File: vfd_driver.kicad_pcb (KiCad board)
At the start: 2 copper layers, 41.1 x 26.7 mm, 23 parts, among them J1 INPUT, J2 FIL, J3 HV, U1 LM4871, U2 LT1073CS

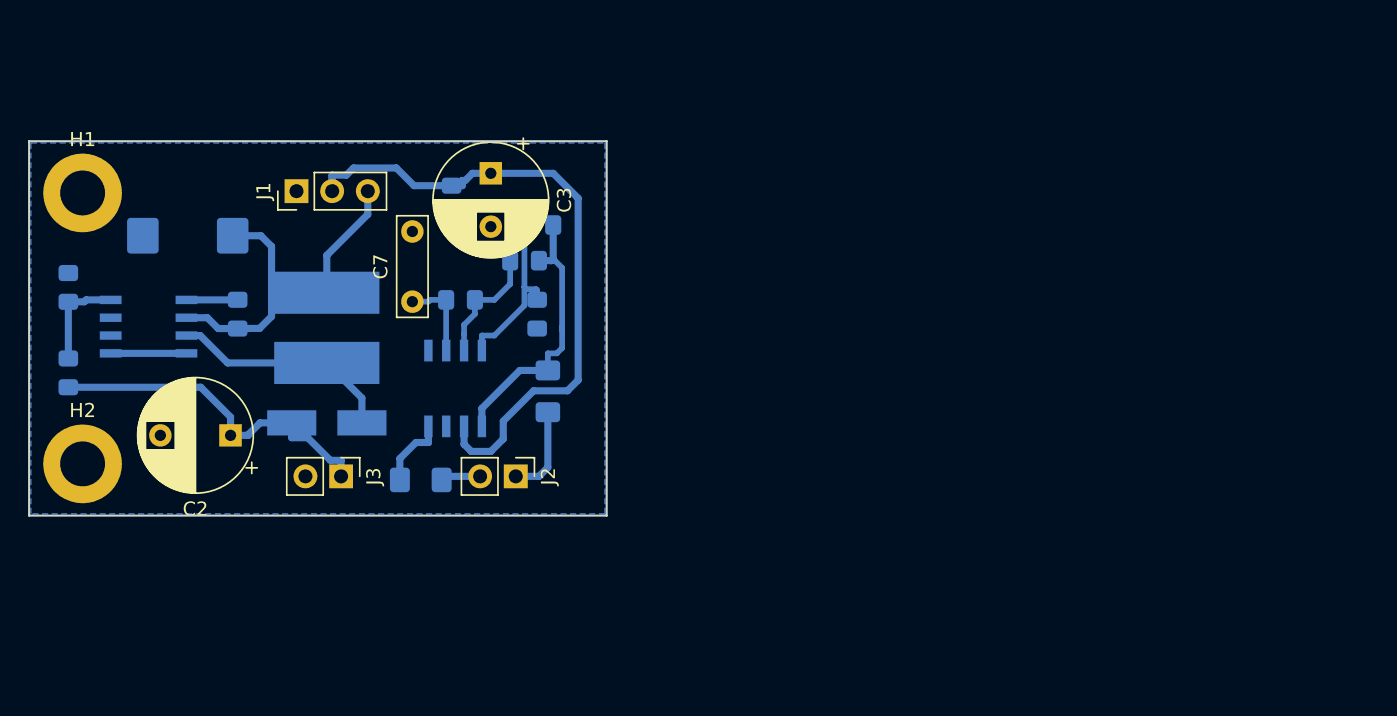
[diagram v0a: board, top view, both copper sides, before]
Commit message: add a protecting diode to the power input. make sure the right thing are pushed.
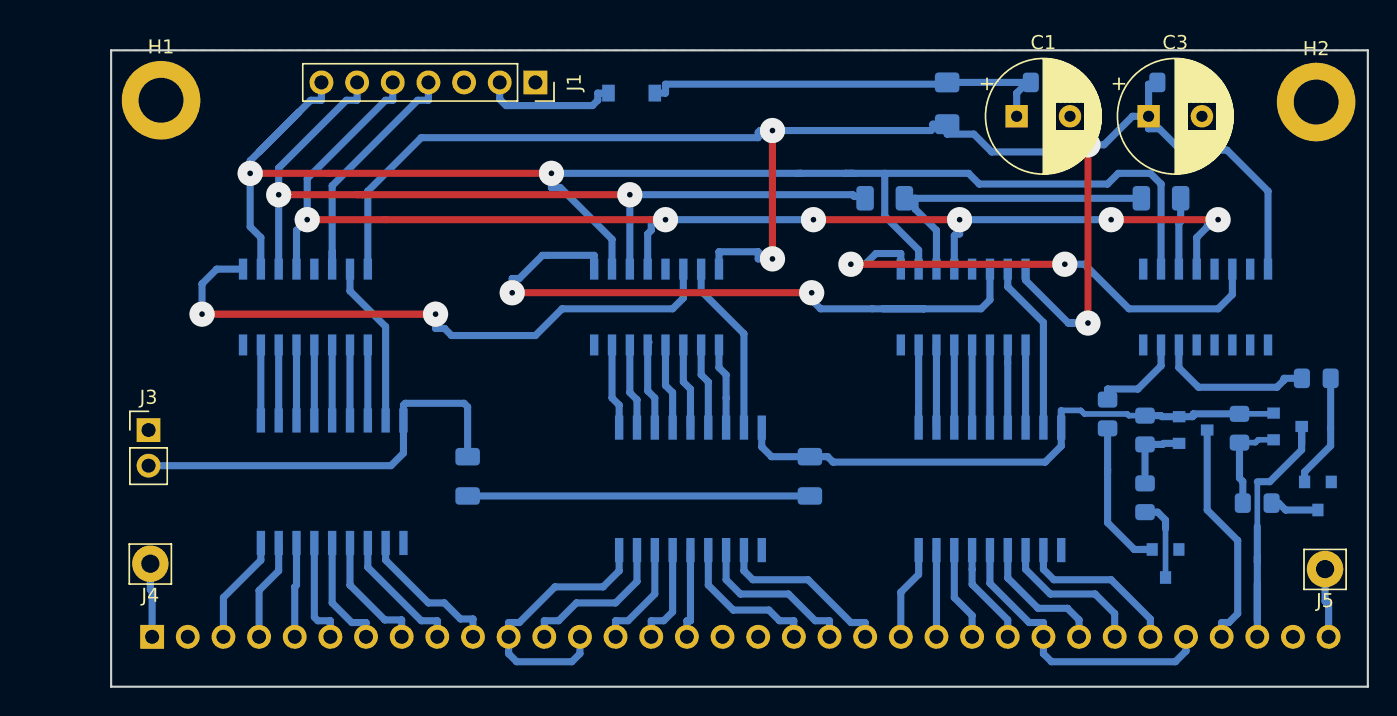
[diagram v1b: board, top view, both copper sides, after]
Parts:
- removed C6: 4n7, Capacitor_SMD:C_0805_2012Metric_Pad1.15x1.40mm_HandSolder
- removed C7: 1u, Capacitor_THT:C_Rect_L7.0mm_W2.0mm_P5.00mm
- removed L1: 330, Choke_SMD:Choke_CD75
- removed R15, R3: 22k, Resistor_SMD:R_0805_2012Metric_Pad1.15x1.40mm_HandSolder
- removed R16, R17: 18, Resistor_SMD:R_1206_3216Metric_Pad1.42x1.75mm_HandSolder
- removed R4: 10k, Resistor_SMD:R_0805_2012Metric_Pad1.15x1.40mm_HandSolder
- added J4: FIL_n, Connector_Pin:Pin_D1.4mm_L8.5mm_W2.8mm_FlatFork, F.Cu at (36.4, 65.5)
- added J5: FIL_p, Connector_Pin:Pin_D1.4mm_L8.5mm_W2.8mm_FlatFork, F.Cu at (120.1, 65.9)
- added L2: 33, Inductor_SMD:L_1206_3216Metric_Pad1.42x1.75mm_HandSolder, B.Cu at (93.2, 32.7)
- added Q3: BC817, Package_TO_SOT_SMD:SOT-23, B.Cu at (119.6, 60.7)
- added Q4: BC807, Package_TO_SOT_SMD:SOT-23, B.Cu at (117.5, 55.8)
- added Q5: BC817, Package_TO_SOT_SMD:SOT-23, B.Cu at (108.8, 65.5)
- added Q6: BC807, Package_TO_SOT_SMD:SOT-23, B.Cu at (110.7, 56.0)
- added R10: 33k, Resistor_SMD:R_0805_2012Metric_Pad1.15x1.40mm_HandSolder, B.Cu at (107.3, 60.8)
- added R12: 0, Resistor_SMD:R_1206_3216Metric, B.Cu at (59.1, 59.3)
- added R13: 0, Resistor_SMD:R_1206_3216Metric, B.Cu at (83.4, 59.3)
- added R6: 100k, Resistor_SMD:R_0805_2012Metric_Pad1.15x1.40mm_HandSolder, B.Cu at (114.0, 55.9)
- added R7: 33k, Resistor_SMD:R_0805_2012Metric_Pad1.15x1.40mm_HandSolder, B.Cu at (115.3, 61.2)
- added R8: 33k, Resistor_SMD:R_0805_2012Metric_Pad1.15x1.40mm_HandSolder, B.Cu at (104.6, 54.9)
- added R9: 100k, Resistor_SMD:R_0805_2012Metric_Pad1.15x1.40mm_HandSolder, B.Cu at (107.3, 56.0)
- added U3: 74HC595, Package_SO:SOIC-16_3.9x9.9mm_P1.27mm, B.Cu at (72.5, 47.2)
- added U4: 74HC595, Package_SO:SOIC-16_3.9x9.9mm_P1.27mm, B.Cu at (94.4, 47.2)
- added U5: TBD62783A, Package_SO:SOP-18_7.0x12.5mm_P1.27mm, B.Cu at (49.4, 59.7)
- added U6: TBD62783A, Package_SO:SOP-18_7.0x12.5mm_P1.27mm, B.Cu at (74.9, 60.2)
- added U7: TBD62783A, Package_SO:SOP-18_7.0x12.5mm_P1.27mm, B.Cu at (96.3, 60.2)
- C1: value 100u -> 10u; footprint Capacitor_Tantalum_SMD:CP_EIA-7343-15_Kemet-W_Pad2.25x2.55mm_HandSolder -> Capacitor_THT:CP_Radial_D8.0mm_P3.80mm; moved to F.Cu
- C2: value 100u/63v -> 100n; footprint Capacitor_THT:CP_Radial_D8.0mm_P5.00mm -> Capacitor_SMD:C_0805_2012Metric_Pad1.15x1.40mm_HandSolder; moved to B.Cu
- C5: value 100n -> 10n
- D1: value SS14 -> SD103BW; footprint Diode_SMD:D_SMA_Handsoldering -> Diode_SMD:D_SOD-123
- J1: value INPUT -> Input; footprint Connector_PinHeader_2.54mm:PinHeader_1x03_P2.54mm_Vertical -> Connector_PinSocket_2.54mm:PinSocket_1x07_P2.54mm_Vertical
- J2: value FIL -> futaba_7_lt_44z; footprint Connector_PinHeader_2.54mm:PinHeader_1x02_P2.54mm_Vertical -> Connector_PinSocket_2.54mm:PinSocket_1x34_P2.54mm_Vertical; moved to B.Cu
- J3: value HV -> High Volt
- R1: value 50 -> 0; footprint Resistor_SMD:R_0805_2012Metric_Pad1.15x1.40mm_HandSolder -> Resistor_SMD:R_1206_3216Metric
- R2: value 1M -> 0; footprint Resistor_SMD:R_0805_2012Metric_Pad1.15x1.40mm_HandSolder -> Resistor_SMD:R_1206_3216Metric
- R5: value 10k -> 33k
- U1: value LM4871 -> 74HC595; footprint Package_SO:SOIC-8_3.9x4.9mm_P1.27mm -> Package_SO:SOIC-16_3.9x9.9mm_P1.27mm
- U2: value LT1073CS -> 74HC595; footprint Package_SO:SOIC-8_3.9x4.9mm_P1.27mm -> Package_SO:SOIC-16_3.9x9.9mm_P1.27mm
- moved H2 91.6 mm to (119.5, 32.6)
- moved R5 89.1 mm to (119.5, 52.3), turned to 0 degrees
- moved R2 78.8 mm to (108.5, 39.5), turned to 0 degrees
- moved C2 63.3 mm to (100.2, 31.2), turned to 0 degrees
- moved C1 59.7 mm to (98.2, 33.7), turned to 0 degrees
- moved U1 53.8 mm to (111.6, 47.2), turned to 90 degrees
- moved C5 52.0 mm to (109.2, 31.2), turned to 0 degrees
- moved C3 47.0 mm to (107.6, 33.7), turned to 0 degrees
- moved R1 46.8 mm to (88.8, 39.5), turned to 0 degrees
- moved D1 32.0 mm to (70.7, 32.0), turned to 180 degrees
- moved J2 28.3 mm to (36.6, 70.7)
- moved J1 18.7 mm to (63.9, 31.2), turned to 270 degrees
- moved J3 14.1 mm to (36.3, 56.0), turned to 0 degrees
- moved U2 11.3 mm to (47.5, 47.2), turned to 90 degrees
- moved H1 8.65 mm to (37.2, 32.5)
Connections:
- C1 pad 1: +12V -> Net-(C1-Pad1)
- C2 pad 1: +36V -> Net-(C1-Pad1)
- C3 pad 1: +5V -> VCC
- C5 pad 1: +5V -> VCC
- D1 pad 1: +36V -> Net-(C1-Pad1)
- D1 pad 2: Net-(D1-Pad2) -> VDD
- J1 pad 2: +5V -> VDD
- J1 pad 3: +12V -> GND
- J2 pad 1: /FIL_n -> Net-(J2-Pad1)
- J2 pad 2: /FIL_p -> (no net)
- J3 pad 1: +36V -> GND
- J3 pad 2: GND -> +36V
- R1 pad 1: Net-(R1-Pad1) -> /SRCLK
- R1 pad 2: +12V -> /SRCLK
- R2 pad 1: Net-(R2-Pad1) -> /SRCLK
- R2 pad 2: +36V -> /SRCLK
- R5 pad 1: GND -> /Q4G
- R5 pad 2: Net-(R2-Pad1) -> Net-(Q3-Pad1)
- U1 pad 1: GND -> (no net)
- U1 pad 2: Net-(C7-Pad1) -> (no net)
- U1 pad 3: Net-(R15-Pad2) -> (no net)
- U1 pad 4: Net-(C6-Pad1) -> (no net)
- U1 pad 5: Net-(R15-Pad1) -> (no net)
- U1 pad 6: +5V -> /Q4G
- U1 pad 7: GND -> /Q4H
- U1 pad 8: Net-(R17-Pad1) -> GND
- U2 pad 1: Net-(R1-Pad1) -> /Q1B
- U2 pad 2: +12V -> /Q1C
- U2 pad 3: Net-(D1-Pad2) -> /Q1D
- U2 pad 4: GND -> /Q1E
- U2 pad 5: GND -> /Q1F
- U2 pad 6: (no net) -> /Q1G
- U2 pad 7: (no net) -> /Q1H
- U2 pad 8: Net-(R2-Pad1) -> GND
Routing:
- net VCC: track 0.00 -> 119.9 mm, vias 0 -> 4
- net /~SRCLR: track 0.00 -> 109.7 mm, vias 0 -> 2
- net /RCLK: track 0.00 -> 94.4 mm, vias 0 -> 6
- net /SRCLK: track 0.00 -> 93.5 mm, vias 0 -> 2
- net +36V: track 25.0 -> 95.8 mm
- net /Q1: track 0.00 -> 48.7 mm, vias 0 -> 2
- net +5V: track 46.8 -> 0.00 mm
- net /Q0: track 0.00 -> 45.6 mm, vias 0 -> 2
- net /Q2: track 0.00 -> 35.3 mm, vias 0 -> 2
- net Net-(C1-Pad1): track 0.00 -> 30.5 mm
- net +12V: track 27.2 -> 0.00 mm
- net Net-(R15-Pad1): track 27.1 -> 0.00 mm
- net /G1: track 0.00 -> 21.3 mm
- net /S10: track 0.00 -> 21.1 mm
- net /G5: track 0.00 -> 19.9 mm
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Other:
- board size 41.1 x 26.7 mm -> 89.5 x 45.3 mm
- board text added: "VFD-DRIVER"

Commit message: remove resistor and align comments
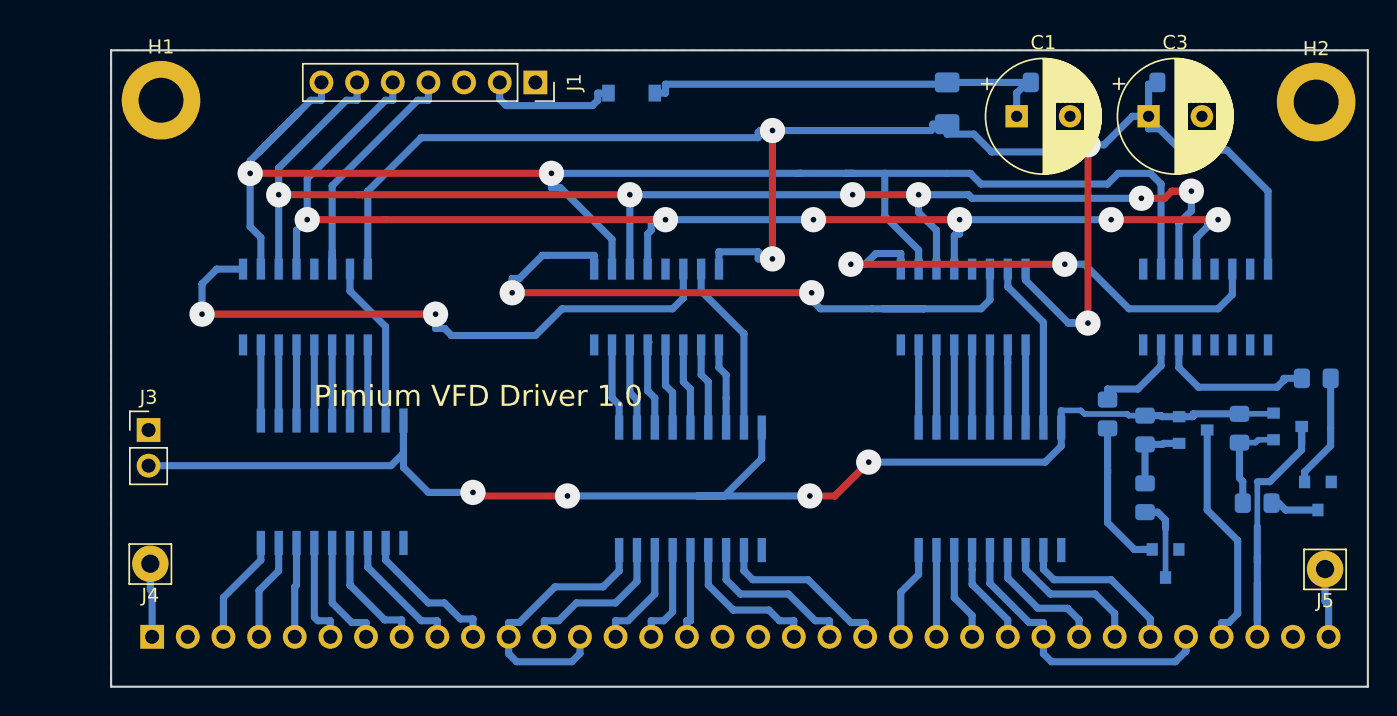
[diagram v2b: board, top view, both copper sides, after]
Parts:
- removed R1, R12, R13, R2: 0, Resistor_SMD:R_1206_3216Metric
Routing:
- net /SRCLK: track 93.5 -> 101.1 mm, vias 2 -> 6
- net +36V: track 95.8 -> 99.9 mm, vias 0 -> 4
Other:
- board text added: "Pimium VFD Driver 1.0"
